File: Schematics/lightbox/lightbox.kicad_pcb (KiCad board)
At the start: 2 copper layers, 5 parts, among them J3 Conn_01x12_Female, U5 D148K, U6 D148K, U7 D148K, U8 D148K

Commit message: Update Schematic and PCB layout
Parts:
- removed U5, U6, U7, U8: D148K, Display_7Segment:D1X8K
- added C1: 0.1µF, Capacitor_THT:CP_Radial_D4.0mm_P1.50mm, F.Cu at (164.5, 94.5)
- added C2: 10µF, Capacitor_THT:CP_Radial_D4.0mm_P1.50mm, F.Cu at (163.5, 98.3)
- added D2: D, Diode_THT:D_A-405_P7.62mm_Horizontal, F.Cu at (133.7, 110.5)
- added D3: D, Diode_THT:D_A-405_P7.62mm_Horizontal, F.Cu at (133.7, 114.0)
- added D4: D, Diode_THT:D_A-405_P7.62mm_Horizontal, F.Cu at (133.7, 117.5)
- added D5: D, Diode_THT:D_A-405_P7.62mm_Horizontal, F.Cu at (133.7, 121.0)
- added J1: Screw_Terminal_01x04, TerminalBlock:TerminalBlock_Altech_AK300-4_P5.00mm, F.Cu at (168.1, 122.1)
- added J2: Conn_01x07_Female, Connector_PinHeader_1.27mm:PinHeader_1x07_P1.27mm_Horizontal, F.Cu at (125.0, 118.5)
- added J5: Conn_02x03_Odd_Even, Connector_PinHeader_1.27mm:PinHeader_2x03_P1.27mm_Vertical, F.Cu at (168.2, 85.1)
- added JP1: Jumper_2_Bridged, Connector_PinHeader_1.27mm:PinHeader_1x02_P1.27mm_Vertical, F.Cu at (154.5, 98.0)
- added Q1: IRF740, Package_TO_SOT_THT:TO-220-3_Vertical, F.Cu at (159.5, 111.5)
- added Q2: IRF740, Package_TO_SOT_THT:TO-220-3_Vertical, F.Cu at (159.5, 122.0)
- added R1: 470R, Resistor_THT:R_Axial_DIN0204_L3.6mm_D1.6mm_P5.08mm_Vertical, F.Cu at (137.8, 97.3)
- added R10: 470R, Resistor_THT:R_Axial_DIN0204_L3.6mm_D1.6mm_P5.08mm_Vertical, F.Cu at (136.5, 124.4)
- added R11: 1K, Resistor_THT:R_Axial_DIN0204_L3.6mm_D1.6mm_P5.08mm_Vertical, F.Cu at (167.0, 102.0)
- added R12: 1.5K, Resistor_THT:R_Axial_DIN0204_L3.6mm_D1.6mm_P5.08mm_Vertical, F.Cu at (169.5, 97.0)
- added R2: 470R, Resistor_THT:R_Axial_DIN0204_L3.6mm_D1.6mm_P5.08mm_Vertical, F.Cu at (137.8, 79.5)
- added R3: 470R, Resistor_THT:R_Axial_DIN0204_L3.6mm_D1.6mm_P5.08mm_Vertical, F.Cu at (137.8, 82.0)
- added R4: 470R, Resistor_THT:R_Axial_DIN0204_L3.6mm_D1.6mm_P5.08mm_Vertical, F.Cu at (137.8, 84.6)
- added R5: 470R, Resistor_THT:R_Axial_DIN0204_L3.6mm_D1.6mm_P5.08mm_Vertical, F.Cu at (137.8, 87.1)
- added R6: 470R, Resistor_THT:R_Axial_DIN0204_L3.6mm_D1.6mm_P5.08mm_Vertical, F.Cu at (137.8, 89.7)
- added R7: 470R, Resistor_THT:R_Axial_DIN0204_L3.6mm_D1.6mm_P5.08mm_Vertical, F.Cu at (137.8, 92.2)
- added R8: 470R, Resistor_THT:R_Axial_DIN0204_L3.6mm_D1.6mm_P5.08mm_Vertical, F.Cu at (137.8, 94.7)
- added R9: 1K, Resistor_THT:R_Axial_DIN0204_L3.6mm_D1.6mm_P5.08mm_Vertical, F.Cu at (139.0, 107.5)
- added U1: ATtiny85-20P, Package_DIP:DIP-8_W7.62mm, F.Cu at (156.9, 79.9)
- added U2: 74AHCT595, Package_DIP:DIP-16_W7.62mm, F.Cu at (142.8, 79.2)
- added U3: 74HC595, Package_DIP:DIP-16_W7.62mm, F.Cu at (145.5, 105.6)
- added U4: LM317_TO-220, Package_TO_SOT_THT:TO-220-3_Vertical, F.Cu at (159.5, 101.0)
- J3: value Conn_01x12_Female -> Conn_01x11_Female
- moved J3 35.2 mm to (125.0, 93.5), turned to 180 degrees
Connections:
- J3 pad 1: /A -> /Digit3
- J3 pad 10: /Digit3 -> /B
- J3 pad 11: /Digit2 -> /A
- J3 pad 12: /Digit1 -> (no net)
- J3 pad 2: /B -> /Digit2
- J3 pad 3: /C -> /Digit1
- J3 pad 4: /D -> /H
- J3 pad 5: /E -> /G
- J3 pad 7: /G -> /E
- J3 pad 8: /H -> /D
- J3 pad 9: /Digit4 -> /C
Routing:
- net /G: track 148.6 -> 10.3 mm, vias 4 -> 0
- net /F: track 106.6 -> 9.76 mm, vias 4 -> 0
- net /Keypad: track 0.00 -> 86.1 mm
- net /C: track 90.3 -> 8.18 mm, vias 4 -> 0
- net /D: track 84.7 -> 8.71 mm, vias 4 -> 0
- net +3V3: track 0.00 -> 69.7 mm
- net /E: track 76.6 -> 9.24 mm, vias 4 -> 0
- net /UVLeds: track 0.00 -> 65.2 mm
- net /A: track 64.5 -> 8.21 mm, vias 4 -> 0
- net /B: track 57.8 -> 7.68 mm, vias 4 -> 0
- net /H: track 60.5 -> 10.9 mm, vias 4 -> 0
- net /Rclk: track 0.00 -> 40.8 mm
- net +12V: track 0.00 -> 40.4 mm
- net /Clk: track 0.00 -> 38.5 mm
- net /Data: track 0.00 -> 35.8 mm
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- added copper zone on B.Cu, net GND
- added copper zone on F.Cu, net GND
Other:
- board outline added: 50.5 x 57.5 mm

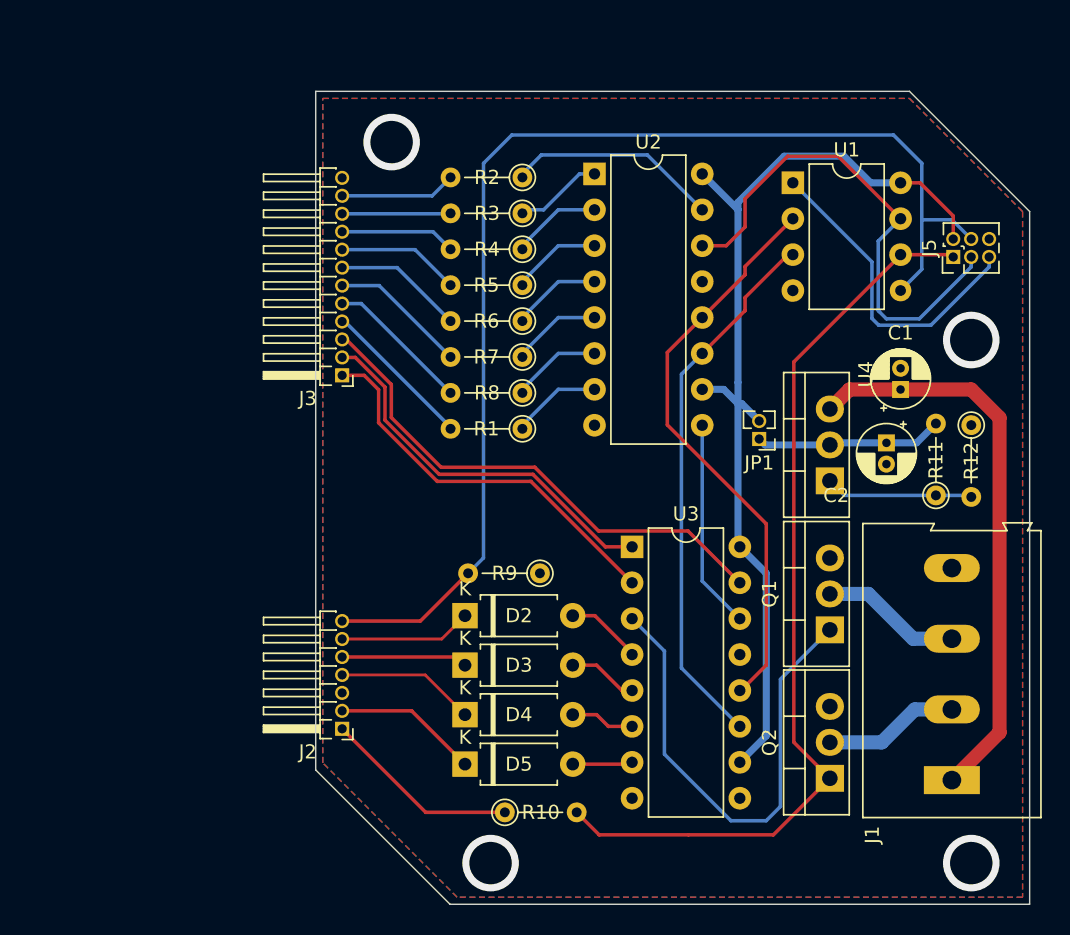
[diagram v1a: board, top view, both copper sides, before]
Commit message: remove unnecessary diodes
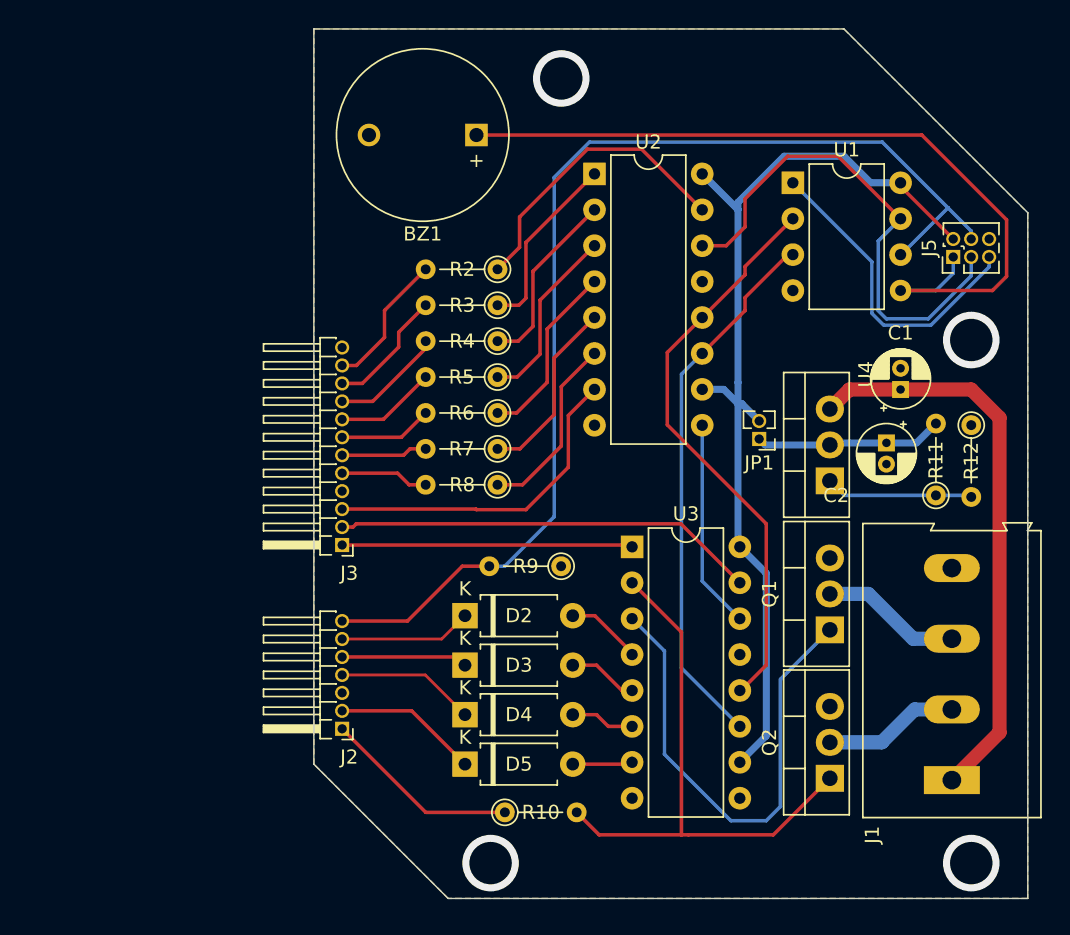
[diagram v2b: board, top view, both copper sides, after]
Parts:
- removed R1: 470R, Resistor_THT:R_Axial_DIN0204_L3.6mm_D1.6mm_P5.08mm_Vertical
- added BZ1: Buzzer, Buzzer_Beeper:MagneticBuzzer_ProSignal_ABI-010-RC, F.Cu at (134.5, 76.5)
- moved J3 12.0 mm to (125.0, 105.5)
- moved R2 6.73 mm to (136.0, 86.0)
- moved R3 6.73 mm to (136.0, 88.5)
- moved R4 6.73 mm to (136.0, 91.1)
- moved R5 6.73 mm to (136.0, 93.6)
- moved R6 6.73 mm to (136.0, 96.2)
- moved R7 6.73 mm to (136.0, 98.7)
- moved R8 6.73 mm to (136.0, 101.2)
- moved R9 1.58 mm to (140.5, 107.0)
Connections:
- J5 pad 1: /UVLeds -> /Buzzer
- U1 pad 5: /Keypad -> /Buzzer
- U1 pad 6: /UVLeds -> /Keypad
- U2 pad 7: Net-(R1-Pad1) -> /Digit1
- U3 pad 1: /Digit2 -> /Digit3
- U3 pad 15: /Digit1 -> /Digit2
- U3 pad 2: /Digit3 -> /UVLeds
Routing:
- net /Buzzer: track 0.00 -> 57.3 mm
- net /UVLeds: track 65.2 -> 39.5 mm
- net /Digit1: track 36.6 -> 23.5 mm
- net /H: track 10.9 -> 0.00 mm
- net /Digit3: track 28.0 -> 20.6 mm
- net Net-(R8-Pad1): track 6.15 -> 13.2 mm
- net Net-(R7-Pad1): track 6.15 -> 13.1 mm
- net Net-(R3-Pad1): track 6.15 -> 13.0 mm
- net Net-(R4-Pad1): track 6.15 -> 13.0 mm
- net Net-(R5-Pad1): track 6.15 -> 12.9 mm
- net Net-(R6-Pad1): track 6.15 -> 12.9 mm
- net Net-(R2-Pad1): track 14.9 -> 21.0 mm
- net Net-(R1-Pad1): track 6.15 -> 0.00 mm
- net /Keypad: track 86.1 -> 80.5 mm
- net /G: track 10.3 -> 6.25 mm
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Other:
- board size 50.5 x 57.5 mm -> 50.5 x 61.5 mm

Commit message: Fix annotations
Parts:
- removed D2, D3, D4, D5: D, Diode_THT:D_A-405_P7.62mm_Horizontal
- moved R8 3.00 mm to (140.5, 110.0)
- renumbered J3 to J2, J2 to J3, J5 to J4, R2 to R1, R11 to R10, R12 to R11, R3 to R2, R4 to R3, R5 to R4, R6 to R5, R7 to R6, R8 to R7, R9 to R8, R10 to R9, U2 to U1, U3 to U2, U1 to U3
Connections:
- U2 pad 4: Net-(D2-Pad2) -> /SW_Push_-
- U2 pad 5: Net-(D3-Pad2) -> /SW_Push_RESET
- U2 pad 6: Net-(D4-Pad2) -> /SW_Push_+
- U2 pad 7: Net-(D5-Pad2) -> /SW_Push_START
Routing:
- net /SW_Push_RESET: track 8.93 -> 21.5 mm
- net /SW_Push_+: track 9.85 -> 22.0 mm
- net /SW_Push_START: track 10.3 -> 22.0 mm
- net /SW_Push_-: track 9.37 -> 21.0 mm
- net Net-(D2-Pad2): track 5.41 -> 0.00 mm
- net Net-(D3-Pad2): track 4.94 -> 0.00 mm
- net Net-(D4-Pad2): track 4.54 -> 0.00 mm
- net Net-(D5-Pad2): track 4.25 -> 0.00 mm
- net /Keypad: track 80.5 -> 81.6 mm

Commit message: Update schematics
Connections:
- J4 pad 1: /Buzzer -> /Keypad
- J4 pad 4: /Keypad -> /Buzzer
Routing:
- net /Buzzer: track 57.3 -> 45.9 mm
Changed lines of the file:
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@@
     (fp_line (start -1.07 3.175) (end -1.07 0.2175) (layer "F.Fab") (width 0.1))
     (pad "1" thru_hole rect (at 0 0 90) (size 1 1) (drill 0.65) (layers *.Cu *.Mask)
-      (net 37 "/Buzzer") (pinfunction "Pin_1") (pintype "passive"))
+      (net 35 "/Keypad") (pinfunction "Pin_1") (pintype "passive"))
     (pad "2" thru_hole oval (at 1.27 0 90) (size 1 1) (drill 0.65) (layers *.Cu *.Mask)
       (net 5 "+3V3") (pinfunction "Pin_2") (pintype "passive"))
@@
       (net 2 "/Data") (pinfunction "Pin_3") (pintype "passive"))
     (pad "4" thru_hole oval (at 1.27 1.27 90) (size 1 1) (drill 0.65) (layers *.Cu *.Mask)
-      (net 35 "/Keypad") (pinfunction "Pin_4") (pintype "passive"))
+      (net 37 "/Buzzer") (pinfunction "Pin_4") (pintype "passive"))
     (pad "5" thru_hole oval (at 0 2.54 90) (size 1 1) (drill 0.65) (layers *.Cu *.Mask)
       (net 34 "/ISP_RST") (pinfunction "Pin_5") (pintype "passive"))
@@
   (segment (start 153.21 115.79) (end 155 114) (width 0.25) (layer "F.Cu") (net 4))
   (segment (start 148 91.88) (end 150.47 89.41) (width 0.25) (layer "F.Cu") (net 4))
-  (segment (start 164.5 80.13) (end 164.5 79.88) (width 0.25) (layer "F.Cu") (net 5))
-  (segment (start 168.225 83.855) (end 164.5 80.13) (width 0.25) (layer "F.Cu") (net 5))
+  (segment (start 164.5 79.88) (end 168.225 83.605) (width 0.25) (layer "F.Cu") (net 5))
   (segment (start 153.27 95.5) (end 154.5 96.73) (width 0.5) (layer "B.Cu") (net 5))
   (segment (start 153 105.5) (end 153.13 105.63) (width 0.5) (layer "B.Cu") (net 5))
@@
   (segment (start 125 110.88) (end 134.53 110.88) (width 0.25) (layer "F.Cu") (net 35))
   (segment (start 134.53 110.88) (end 135.41 110) (width 0.25) (layer "F.Cu") (net 35))
-  (segment (start 167.85515 81.64485) (end 164.54 84.96) (width 0.25) (layer "B.Cu") (net 35))
+  (segment (start 168.06 84.96) (end 168.225 85.125) (width 0.25) (layer "F.Cu") (net 35))
+  (segment (start 164.5 84.96) (end 168.06 84.96) (width 0.25) (layer "F.Cu") (net 35))
   (segment (start 135.41 110) (end 140 105.41) (width 0.25) (layer "B.Cu") (net 35))
-  (segment (start 142.5 77) (end 163.2103 77) (width 0.25) (layer "B.Cu") (net 35))
-  (segment (start 169.495 83.855) (end 169.5 83.85) (width 0.25) (layer "B.Cu") (net 35))
-  (segment (start 169.5 83.85) (end 169.5 83.2897) (width 0.25) (layer "B.Cu") (net 35))
   (segment (start 140 79.5) (end 142.5 77) (width 0.25) (layer "B.Cu") (net 35))
-  (segment (start 163.2103 77) (end 167.85515 81.64485) (width 0.25) (layer "B.Cu") (net 35))
-  (segment (start 169.5 83.2897) (end 167.85515 81.64485) (width 0.25) (layer "B.Cu") (net 35))
-  (segment (start 164.54 84.96) (end 164.5 84.96) (width 0.25) (layer "B.Cu") (net 35))
+  (segment (start 166.5 80) (end 166.5 82.96) (width 0.25) (layer "B.Cu") (net 35))
   (segment (start 140 105.41) (end 140 79.5) (width 0.25) (layer "B.Cu") (net 35))
+  (segment (start 163.5 77) (end 166.5 80) (width 0.25) (layer "B.Cu") (net 35))
+  (segment (start 142.5 77) (end 163.5 77) (width 0.25) (layer "B.Cu") (net 35))
+  (segment (start 166.5 82.96) (end 164.5 84.96) (width 0.25) (layer "B.Cu") (net 35))
   (segment (start 152.5 125) (end 155 125) (width 0.25) (layer "B.Cu") (net 36))
   (segment (start 147.8 113) (end 147.8 120.3) (width 0.25) (layer "B.Cu") (net 36))
@@
   (segment (start 147.8 120.3) (end 152.5 125) (width 0.25) (layer "B.Cu") (net 36))
   (segment (start 145.51 110.71) (end 147.8 113) (width 0.25) (layer "B.Cu") (net 36))
-  (segment (start 172 86.5) (end 172 82.5) (width 0.25) (layer "F.Cu") (net 37))
-  (segment (start 171 87.5) (end 172 86.5) (width 0.25) (layer "F.Cu") (net 37))
-  (segment (start 164.5 87.5) (end 171 87.5) (width 0.25) (layer "F.Cu") (net 37))
-  (segment (start 172 82.5) (end 166 76.5) (width 0.25) (layer "F.Cu") (net 37))
-  (segment (start 166 76.5) (end 134.5 76.5) (width 0.25) (layer "F.Cu") (net 37))
-  (segment (start 168.225 86.275) (end 168.225 85.125) (width 0.25) (layer "B.Cu") (net 37))
-  (segment (start 164.5 87.5) (end 167 87.5) (width 0.25) (layer "B.Cu") (net 37))
-  (segment (start 167 87.5) (end 168.225 86.275) (width 0.25) (layer "B.Cu") (net 37))
+  (segment (start 166.94952 81.94952) (end 166.94952 79.813802) (width 0.25) (layer "B.Cu") (net 37))
+  (segment (start 163.635718 76.5) (end 134.5 76.5) (width 0.25) (layer "B.Cu") (net 37))
+  (segment (start 166.94952 79.813802) (end 163.635718 76.5) (width 0.25) (layer "B.Cu") (net 37))
+  (segment (start 166.94952 85.05048) (end 166.94952 81.94952) (width 0.25) (layer "B.Cu") (net 37))
+  (segment (start 166.94952 81.94952) (end 167.58952 81.94952) (width 0.25) (layer "B.Cu") (net 37))
+  (segment (start 164.5 87.5) (end 166.94952 85.05048) (width 0.25) (layer "B.Cu") (net 37))
+  (segment (start 167.58952 81.94952) (end 169.495 83.855) (width 0.25) (layer "B.Cu") (net 37))
   (segment (start 137.55048 84.44952) (end 137.55048 82.300498) (width 0.25) (layer "F.Cu") (net 38))
   (segment (start 137.55048 82.300498) (end 142.350978 77.5) (width 0.25) (layer "F.Cu") (net 38))

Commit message: Revert schematics
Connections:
- net /Data renamed /D_{2}
- net /Keypad renamed /D_{1}
- net /Rclk renamed /D_{3}

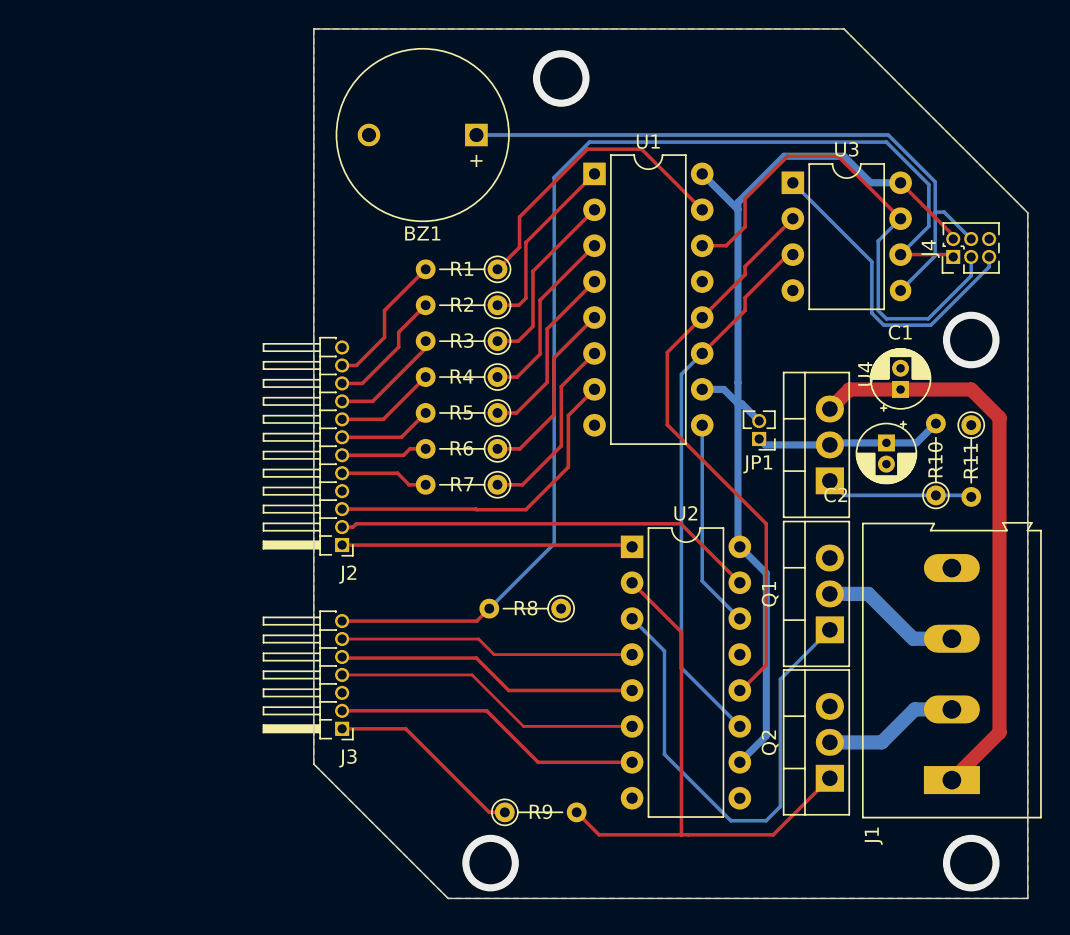
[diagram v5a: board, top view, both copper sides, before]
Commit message: Update PCB Layout; Update Regulator design
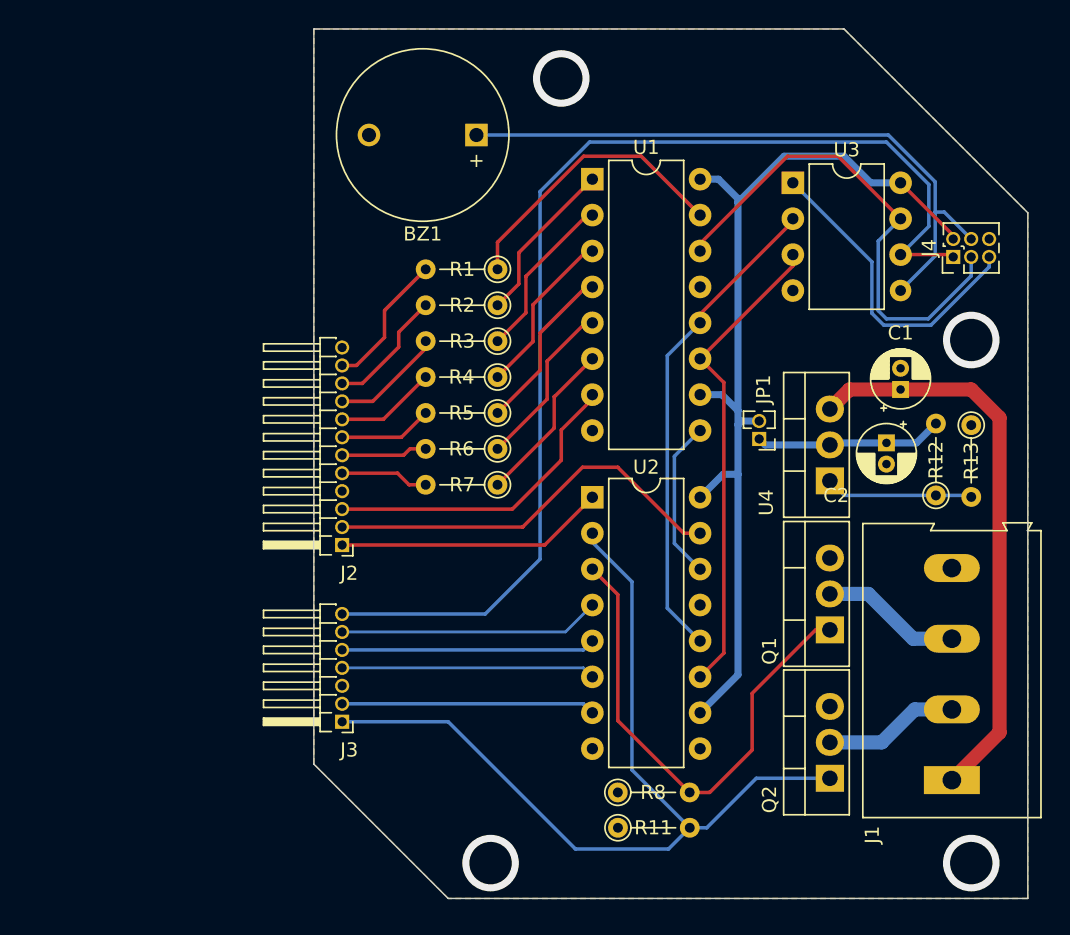
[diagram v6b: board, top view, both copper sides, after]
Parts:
- removed R9: 470R, Resistor_THT:R_Axial_DIN0204_L3.6mm_D1.6mm_P5.08mm_Vertical
- added R11: 10K, Resistor_THT:R_Axial_DIN0204_L3.6mm_D1.6mm_P5.08mm_Vertical, F.Cu at (144.5, 125.5)
- R12: renamed from R10; value 1K -> 100
- R13: renamed from R11; value 1.5K -> 220
- R8: value 1K -> 10K
- moved R8 13.6 mm to (144.5, 123.0), turned to 0 degrees
- moved U2 4.49 mm to (142.7, 102.1)
- moved J3 0.50 mm to (125.0, 118.0)
- moved U1 0.40 mm to (142.7, 79.6)
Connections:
- J3 pad 1: /Led -> /UVLeds
- R8 pad 2: /D_{1} -> /REDLeds
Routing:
- net /UVLeds: track 39.5 -> 64.0 mm
- net /Led: track 14.0 -> 0.00 mm
- net /D_{3}: track 40.8 -> 34.5 mm
- net /Clk: track 38.5 -> 34.0 mm
- net /SW_Push_START: track 22.0 -> 18.0 mm
- net /SW_Push_+: track 22.0 -> 18.0 mm
- net /SW_Push_RESET: track 21.5 -> 18.0 mm
- net /QH': track 14.8 -> 11.3 mm
- net /SW_Push_-: track 21.0 -> 18.5 mm
- net /Digit3: track 20.6 -> 19.1 mm
- net Net-(R7-Pad1): track 13.2 -> 11.7 mm
- net Net-(R2-Pad1): track 13.0 -> 11.7 mm
- net Net-(R3-Pad1): track 13.0 -> 11.9 mm
- net Net-(R6-Pad1): track 13.1 -> 12.0 mm
- net /Digit1: track 23.5 -> 22.5 mm
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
